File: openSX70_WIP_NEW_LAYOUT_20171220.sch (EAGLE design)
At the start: 39 parts, among them Q1 5.8A/30V/35mΩ, Q2 5.8A/30V/35mΩ, U1 ATMEGA328P_TQFP, U3 BH1750FVI-TR, Y1 CSTCE16M0V53-R0

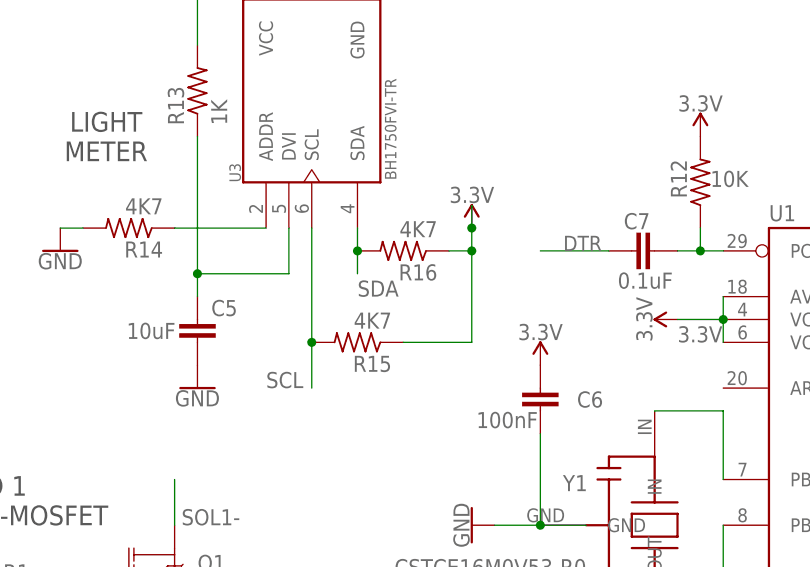
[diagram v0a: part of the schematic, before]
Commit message: minor updates in new layout. Routing manually important traces.
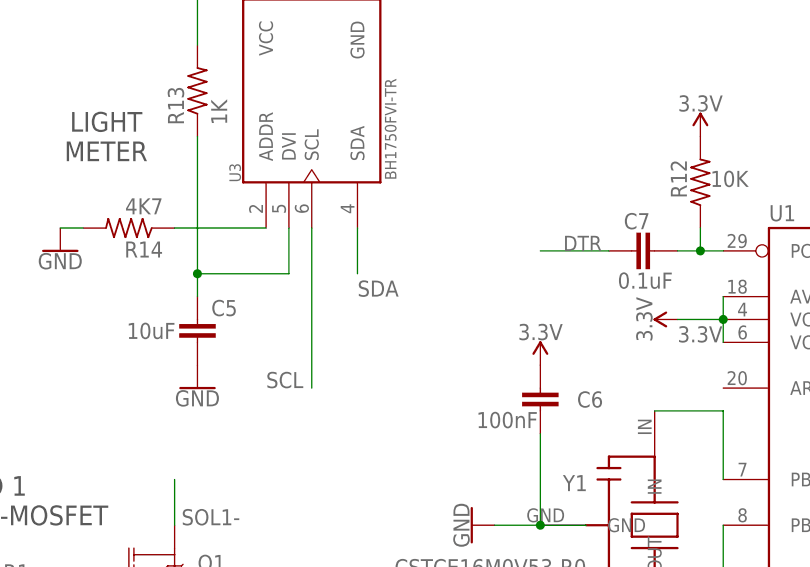
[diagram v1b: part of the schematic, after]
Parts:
- removed R15, R16: 4K7, resistor:R-US_R0603
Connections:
- net 3.3V: no longer R15.1, R16.1
- net SCL: no longer R15.2
- net SDA: no longer R16.2
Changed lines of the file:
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@@
 <part name="GND20" library="SparkFun-PowerSymbols" library_urn="urn:adsk.eagle:library:530" deviceset="GND" device=""/>
 <part name="R14" library="resistor" library_urn="urn:adsk.eagle:library:348" deviceset="R-US_" device="R0603" package3d_urn="urn:adsk.eagle:package:26057/1" value="4K7"/>
-<part name="R15" library="resistor" library_urn="urn:adsk.eagle:library:348" deviceset="R-US_" device="R0603" package3d_urn="urn:adsk.eagle:package:26057/1" value="4K7"/>
-<part name="R16" library="resistor" library_urn="urn:adsk.eagle:library:348" deviceset="R-US_" device="R0603" package3d_urn="urn:adsk.eagle:package:26057/1" value="4K7"/>
-<part name="SUPPLY8" library="SparkFun-PowerSymbols" library_urn="urn:adsk.eagle:library:530" deviceset="3.3V" device=""/>
 <part name="P+6" library="openSX70" deviceset="VCC" device="" value="6V"/>
 <part name="Y1" library="CSTCE16M0V53-R0" deviceset="CSTCE16M0V53-R0" device=""/>
@@
 <instance part="GND20" gate="1" x="86.36" y="111.76"/>
 <instance part="R14" gate="G$1" x="78.74" y="129.54" rot="R180"/>
-<instance part="R15" gate="G$1" x="104.14" y="116.84" rot="R180"/>
-<instance part="R16" gate="G$1" x="109.22" y="127" rot="R180"/>
-<instance part="SUPPLY8" gate="G$1" x="116.84" y="129.54"/>
 <instance part="P+6" gate="VCC" x="208.28" y="149.86" rot="R270"/>
 <instance part="Y1" gate="G$1" x="132.08" y="96.52" smashed="yes" rot="R270">
@@
 <segment>
 <pinref part="U3" gate="G$1" pin="SDA"/>
-<wire x1="104.14" y1="129.54" x2="104.14" y2="127" width="0.1524" layer="91"/>
 <label x="104.14" y="121.92" size="1.778" layer="95"/>
-<pinref part="R16" gate="G$1" pin="2"/>
-<wire x1="104.14" y1="127" x2="104.14" y2="124.46" width="0.1524" layer="91"/>
-<junction x="104.14" y="127"/>
+<wire x1="104.14" y1="129.54" x2="104.14" y2="124.46" width="0.1524" layer="91"/>
 </segment>
 </net>
@@
 <wire x1="86.36" y1="162.56" x2="93.98" y2="162.56" width="0.1524" layer="91"/>
 <junction x="93.98" y="162.56"/>
-</segment>
-<segment>
-<pinref part="SUPPLY8" gate="G$1" pin="3.3V"/>
-<wire x1="116.84" y1="129.54" x2="116.84" y2="132.08" width="0.1524" layer="91"/>
-<pinref part="R15" gate="G$1" pin="1"/>
-<wire x1="109.22" y1="116.84" x2="116.84" y2="116.84" width="0.1524" layer="91"/>
-<wire x1="116.84" y1="116.84" x2="116.84" y2="127" width="0.1524" layer="91"/>
-<junction x="116.84" y="129.54"/>
-<pinref part="R16" gate="G$1" pin="1"/>
-<wire x1="116.84" y1="127" x2="116.84" y2="129.54" width="0.1524" layer="91"/>
-<wire x1="114.3" y1="127" x2="116.84" y2="127" width="0.1524" layer="91"/>
-<junction x="116.84" y="127"/>
 </segment>
 </net>
@@
 <segment>
 <pinref part="U3" gate="G$1" pin="SCL"/>
-<wire x1="99.06" y1="129.54" x2="99.06" y2="116.84" width="0.1524" layer="91"/>
+<wire x1="99.06" y1="129.54" x2="99.06" y2="111.76" width="0.1524" layer="91"/>
 <label x="93.98" y="111.76" size="1.778" layer="95"/>
-<pinref part="R15" gate="G$1" pin="2"/>
-<wire x1="99.06" y1="116.84" x2="99.06" y2="111.76" width="0.1524" layer="91"/>
-<junction x="99.06" y="116.84"/>
-</segment>
-</net>
+</segment>
+</net>
